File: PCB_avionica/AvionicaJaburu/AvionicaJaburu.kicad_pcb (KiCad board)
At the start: 2 copper layers, 29 parts, among them J1 Screw_Terminal_01x02, J2 Screw_Terminal_01x02, J3 RESET, J4 Conn_01x08_Pin, J5 VDD, Q1 NMOS_Substrate, Q2 NMOS_Substrate, U1 AMS1117-3.3, U2 ESP32-DEVKIT-V1

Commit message: Aviônica Jaburu pino buzzer atualizado
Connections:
- U2 pad 20: BZR -> unconnected-(U2-D35-Pad20)
- U2 pad 22: unconnected-(U2-D33-Pad22) -> BZR
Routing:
- net GND: track 263.4 -> 0.00 mm
- net BZR: track 14.1 -> 19.1 mm
- net LedStatus: track 48.6 -> 51.4 mm
- net SCL: track 37.5 -> 36.0 mm
- net +3V3: track 175.8 -> 174.6 mm
- net Net-(D1-K): track 38.2 -> 37.3 mm
- net IGN_2: track 14.1 -> 13.3 mm, vias 1 -> 0
- net ADC_BATT: track 80.0 -> 79.1 mm
- net IGN_1: vias 1 -> 0
- net (no net): vias 4 -> 0
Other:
- board text added: "RBF"

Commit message: Aviônica com furações e MOSFET atualizados
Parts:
- added H1: MountingHole, MountingHole:MountingHole_3.2mm_M3, F.Cu at (103.0, 60.0)
- added H2: MountingHole, MountingHole:MountingHole_3.2mm_M3, F.Cu at (192.0, 62.0)
- added H3: MountingHole, MountingHole:MountingHole_3.2mm_M3, F.Cu at (192.0, 112.0)
- added H4: MountingHole, MountingHole:MountingHole_3.2mm_M3, F.Cu at (105.0, 114.0)
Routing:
- net IGN_1: track 31.3 -> 33.8 mm
- net IGN_2: track 13.3 -> 15.8 mm
- net +BATT: track 68.7 -> 70.3 mm
- net ADC_BATT: track 79.1 -> 79.9 mm
- net GND: vias 0 -> 18

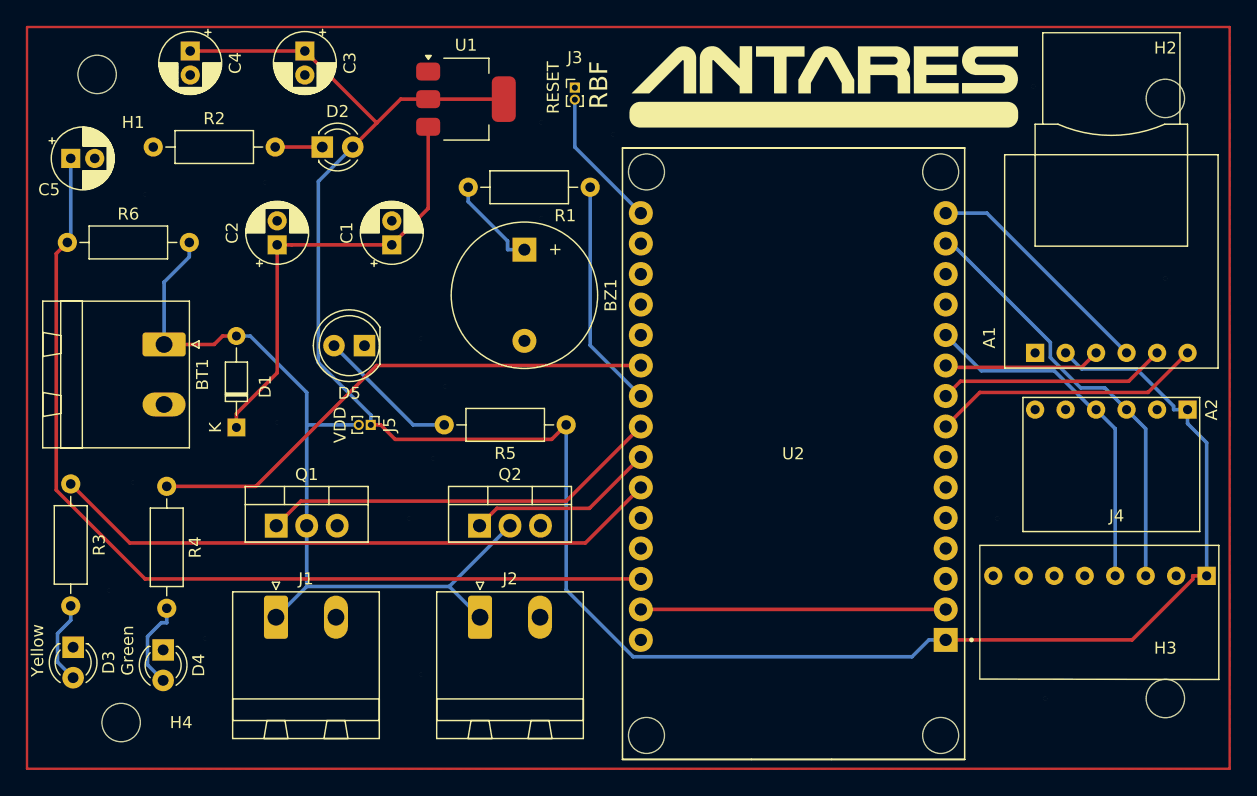
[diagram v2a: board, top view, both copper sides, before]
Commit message: Mudanças no footprint do esp32 na aviônica - retirei os mounting holes do footprint do esp32
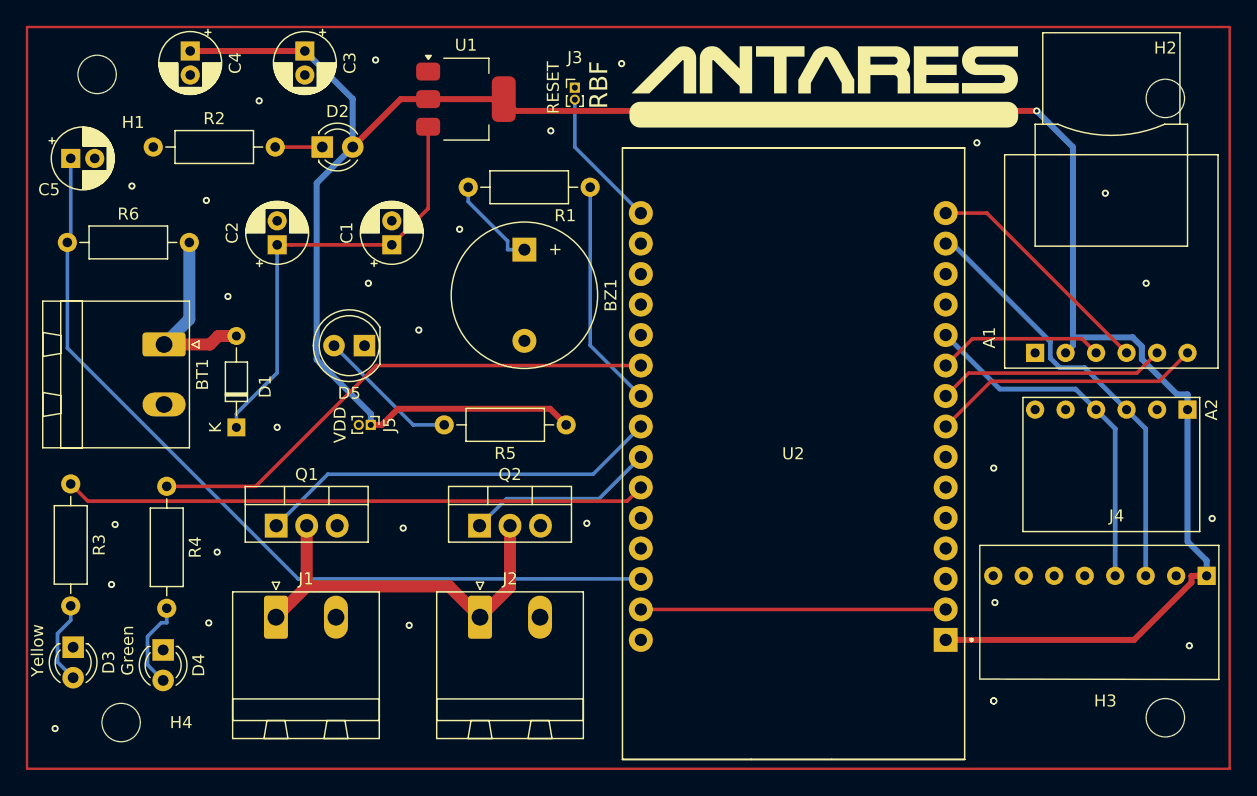
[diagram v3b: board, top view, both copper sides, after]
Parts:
- moved H3 1.60 mm to (192.0, 113.6)
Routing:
- net +BATT: track 70.3 -> 48.5 mm
- net +3V3: track 174.9 -> 195.8 mm, vias 0 -> 1
- net ADC_BATT: track 79.9 -> 71.7 mm
- net LedStatus: track 51.5 -> 48.6 mm
- net MISO: track 13.1 -> 13.9 mm
- net GND: vias 18 -> 28
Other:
- board text added: "Aviônica Jaburu V1.3 Antares Foguetemodelismo Autor: João Estima"
- board text removed: "Aviônica Jaburu V1.1 Antares Foguetemodelismo Autor: João Estima"

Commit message: Adicionado bypass na alimentaçção dos módulos da avionica Jaburu
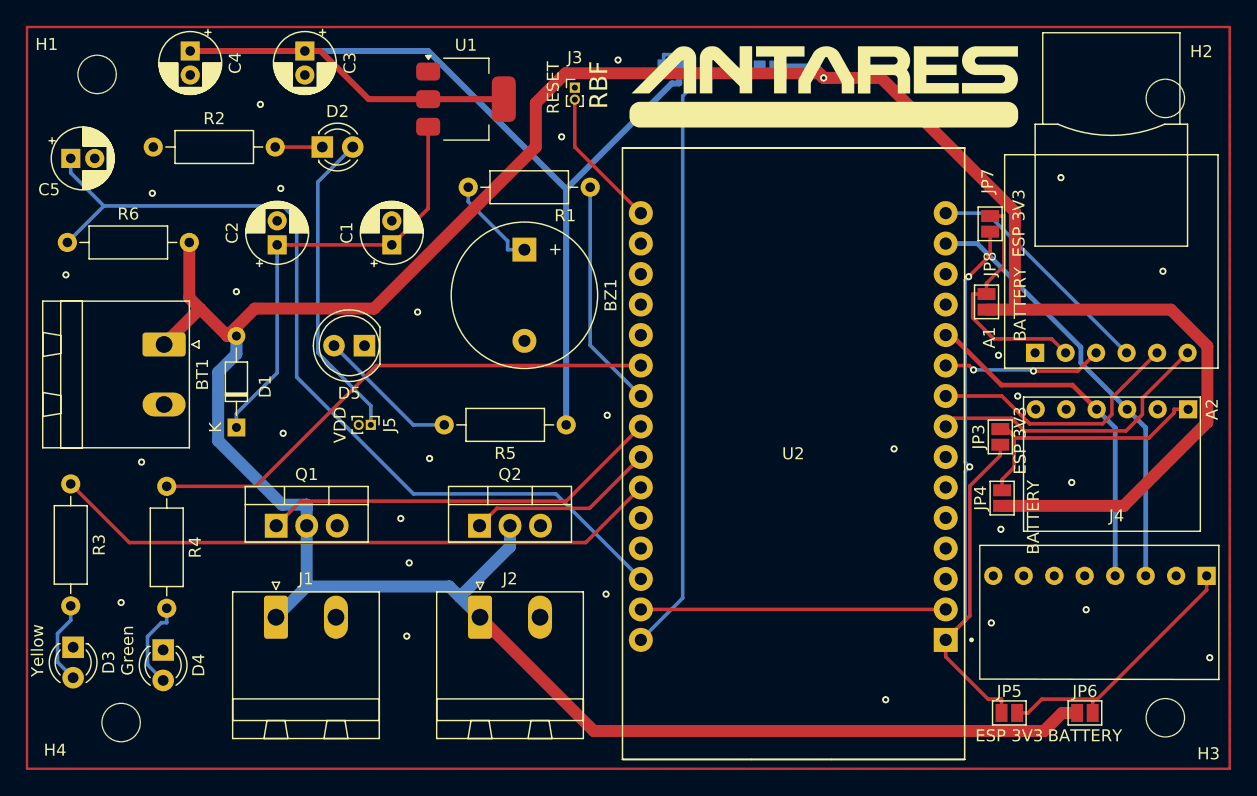
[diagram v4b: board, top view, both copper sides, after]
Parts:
- added JP1: LDO 3V3, Jumper:SolderJumper-2_P1.3mm_Open_Pad1.0x1.5mm, B.Cu at (150.8, 59.5)
- added JP2: BATTERY, Jumper:SolderJumper-2_P1.3mm_Open_Pad1.0x1.5mm, B.Cu at (158.8, 59.6)
- added JP3: ESP 3V3, Jumper:SolderJumper-2_P1.3mm_Open_Pad1.0x1.5mm, F.Cu at (178.2, 90.2)
- added JP4: BATTERY, Jumper:SolderJumper-2_P1.3mm_Open_Pad1.0x1.5mm, F.Cu at (178.4, 95.3)
- added JP5: ESP 3V3, Jumper:SolderJumper-2_P1.3mm_Open_Pad1.0x1.5mm, F.Cu at (179.0, 113.2)
- added JP6: BATTERY, Jumper:SolderJumper-2_P1.3mm_Open_Pad1.0x1.5mm, F.Cu at (185.3, 113.2)
- added JP7: ESP 3V3, Jumper:SolderJumper-2_P1.3mm_Open_Pad1.0x1.5mm, F.Cu at (177.4, 72.5)
- added JP8: BATTERY, Jumper:SolderJumper-2_P1.3mm_Open_Pad1.0x1.5mm, F.Cu at (177.1, 79.0)
- moved A2 0.06 mm to (193.9, 87.9)
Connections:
- A1 pad 2: +3V3 -> Net-(A1-3V3)
- A2 pad 1: +3V3 -> Net-(A2-VCC)
- D2 pad 2: +3V3 -> Net-(D2-A)
- J4 pad 1: +3V3 -> Net-(J4-Pin_1)
- J5 pad 1: +3V3 -> Net-(D2-A)
- U2 pad 1: +3V3 -> VDD
- U2 pad 30: unconnected-(U2-VIN-Pad30) -> Net-(JP1-B)
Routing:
- net +BATT: track 48.5 -> 261.0 mm, vias 0 -> 1
- net +3V3: track 195.8 -> 88.3 mm, vias 1 -> 0
- net VDD: track 0.00 -> 62.7 mm, vias 0 -> 2
- net Net-(JP1-B): track 0.00 -> 59.5 mm
- net Net-(D2-A): track 0.00 -> 26.2 mm
- net Net-(J4-Pin_1): track 0.00 -> 22.4 mm
- net Net-(A2-VCC): track 0.00 -> 22.0 mm
- net Net-(A1-3V3): track 0.00 -> 20.3 mm
- net ADC_BATT: track 71.7 -> 74.7 mm
- net LedStatus: track 48.6 -> 51.4 mm
- net SCK: track 19.1 -> 21.8 mm
- net CSSD: track 22.7 -> 24.4 mm
- net MISO: track 13.9 -> 13.3 mm, vias 0 -> 2
- net GND: vias 28 -> 0
- net (no net): vias 0 -> 28

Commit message: outline da Jaburu corrigido pra fabricação
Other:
- board outline added: 100.2 x 61.8 mm
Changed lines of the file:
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@@
 		(end 197.3574 117.8501)
 		(stroke
-			(width 0.2)
+			(width 0.5)
 			(type default)
 		)
@@
 		(layer "F.SilkS")
 	)
+	(gr_rect
+		(start 97.1574 56.0501)
+		(end 197.3574 117.8501)
+		(stroke
+			(width 0.5)
+			(type default)
+		)
+		(fill none)
+		(layer "Edge.Cuts")
+	)
 	(gr_text "Aviônica Jaburu V1.3\n\nAntares Foguetemodelismo\nAutor: João Estima"

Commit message: correção na diferença entre o clearence e o furo metálico que deve ser >= 0.2mm
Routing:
- net +BATT: track 261.0 -> 241.4 mm, vias 1 -> 0
- net +3V3: track 88.3 -> 72.3 mm
- net ADC_BATT: track 74.7 -> 69.1 mm
- net VDD: track 62.7 -> 66.9 mm, vias 2 -> 0
- net Net-(A1-3V3): track 20.3 -> 16.6 mm
- net SCL: track 36.1 -> 39.7 mm
- net Net-(A2-VCC): track 22.0 -> 25.3 mm
- net MOSI: track 19.9 -> 23.1 mm
- net CSSD: track 24.4 -> 27.4 mm
- net Net-(JP1-B): track 59.5 -> 56.8 mm
- net Net-(J4-Pin_1): track 22.4 -> 23.5 mm
- net LedAcionamento: track 43.7 -> 44.7 mm
- net MISO: track 13.3 -> 13.9 mm, vias 2 -> 0
- net GND: vias 0 -> 19
- net (no net): vias 28 -> 0
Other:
- board text added: "Aviônica Jaburu V1.4 Antares Foguetemodelismo Made by João Estima"
- board text removed: "Aviônica Jaburu V1.3 Antares Foguetemodelismo Autor: João Estima"

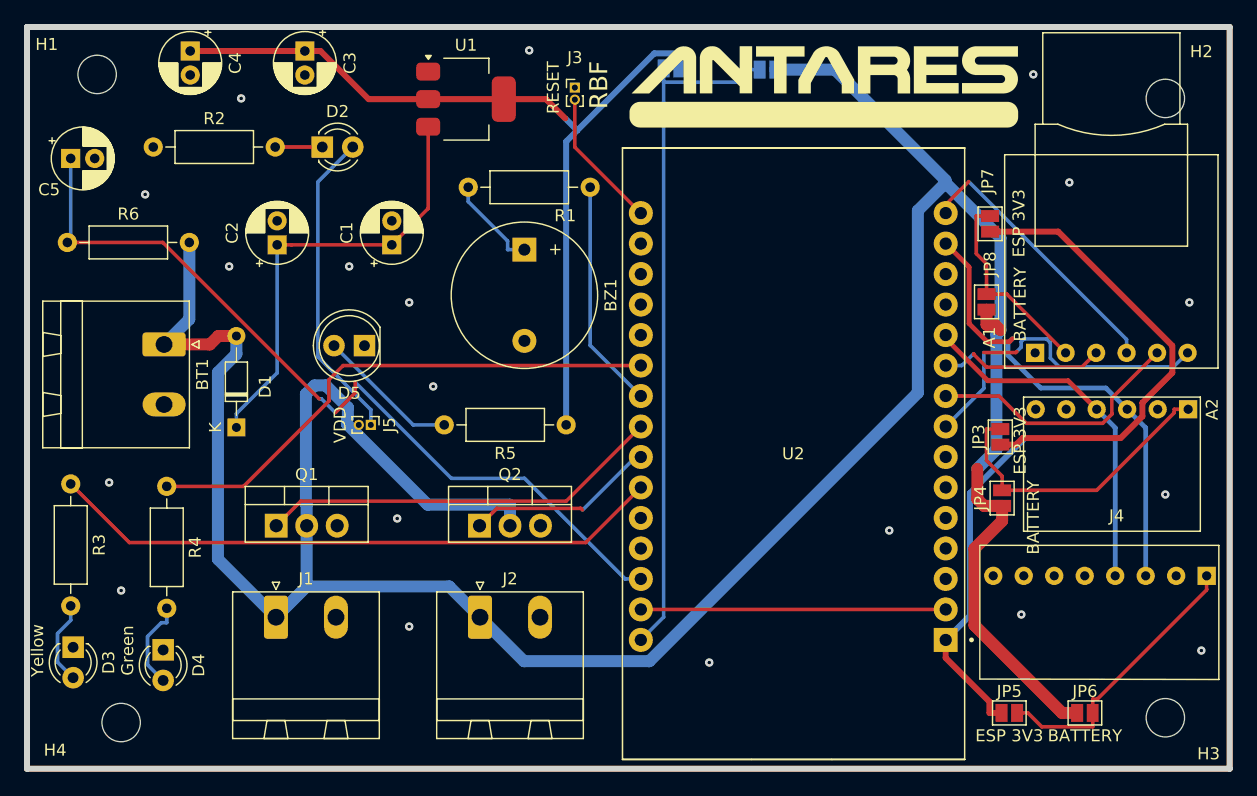
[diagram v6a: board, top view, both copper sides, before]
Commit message: tirei qualquer pinheader com diametro menor que 2.54mm pq a fabricante não aceita
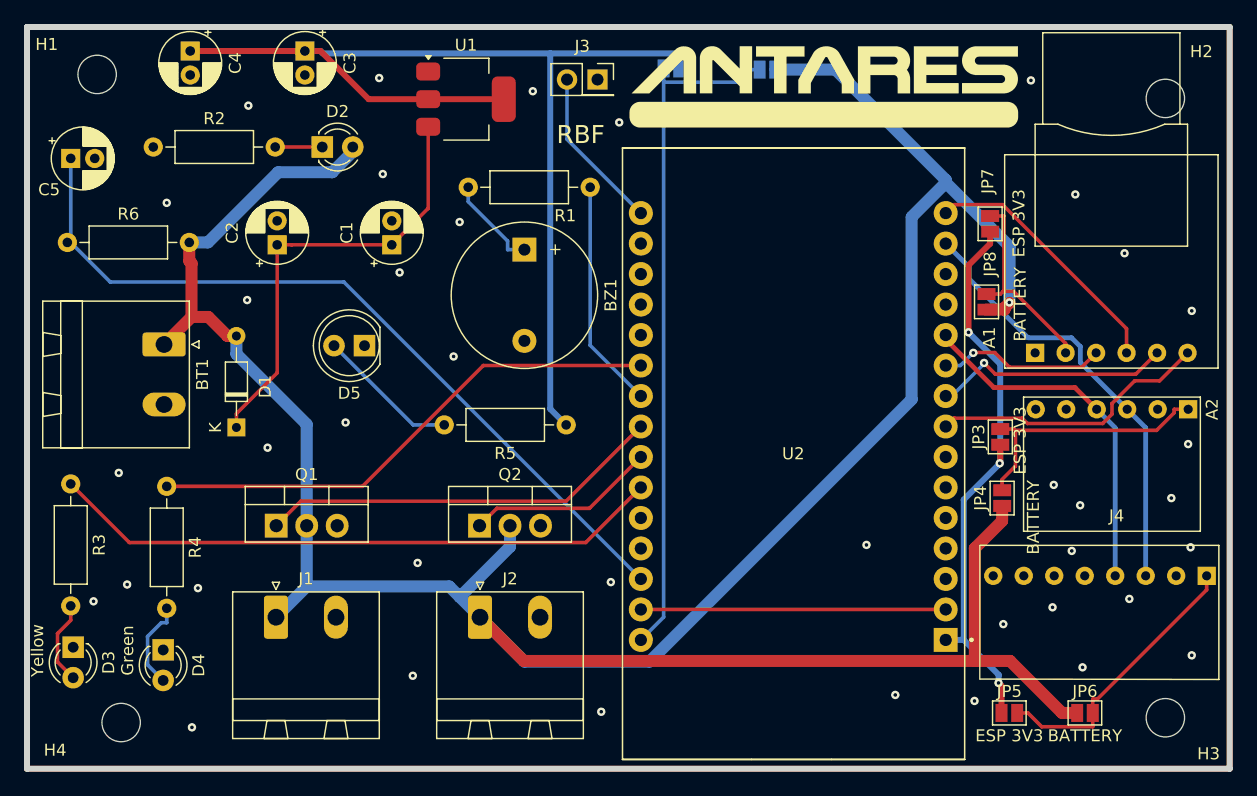
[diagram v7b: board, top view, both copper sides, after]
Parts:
- removed J5: VDD, Connector_PinHeader_1.00mm:PinHeader_1x02_P1.00mm_Vertical
- J3: footprint Connector_PinHeader_1.00mm:PinHeader_1x02_P1.00mm_Vertical -> Connector_PinSocket_2.54mm:PinSocket_2x01_P2.54mm_Vertical
- moved J3 2.01 mm to (144.7, 60.4)
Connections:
- D2 pad 2: Net-(D2-A) -> +BATT
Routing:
- net Net-(D2-A): track 26.2 -> 0.00 mm
- net +3V3: track 72.3 -> 91.8 mm
- net VDD: track 66.9 -> 47.9 mm, vias 0 -> 3
- net +BATT: track 241.4 -> 246.5 mm, vias 0 -> 1
- net CSSD: track 27.4 -> 23.6 mm
- net Net-(A2-VCC): track 25.3 -> 22.0 mm
- net SCL: track 39.7 -> 36.7 mm
- net ADC_BATT: track 69.1 -> 66.4 mm
- net EN: track 11.7 -> 13.7 mm
- net SCK: track 21.8 -> 19.9 mm, vias 0 -> 1
- net MOSI: track 23.1 -> 21.7 mm
- net LedAcionamento: track 44.7 -> 43.7 mm
- net MISO: track 13.9 -> 14.0 mm, vias 0 -> 1
- net GND: vias 19 -> 39
